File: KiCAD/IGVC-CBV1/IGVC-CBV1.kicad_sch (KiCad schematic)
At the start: 29 parts, among them IC1 STM32F407ZGT6, J1 STLINKV2 PINS (2.54mm Pitch), SW1 SW_SPDT, Y1 EB2532YA12-25.000M_TR

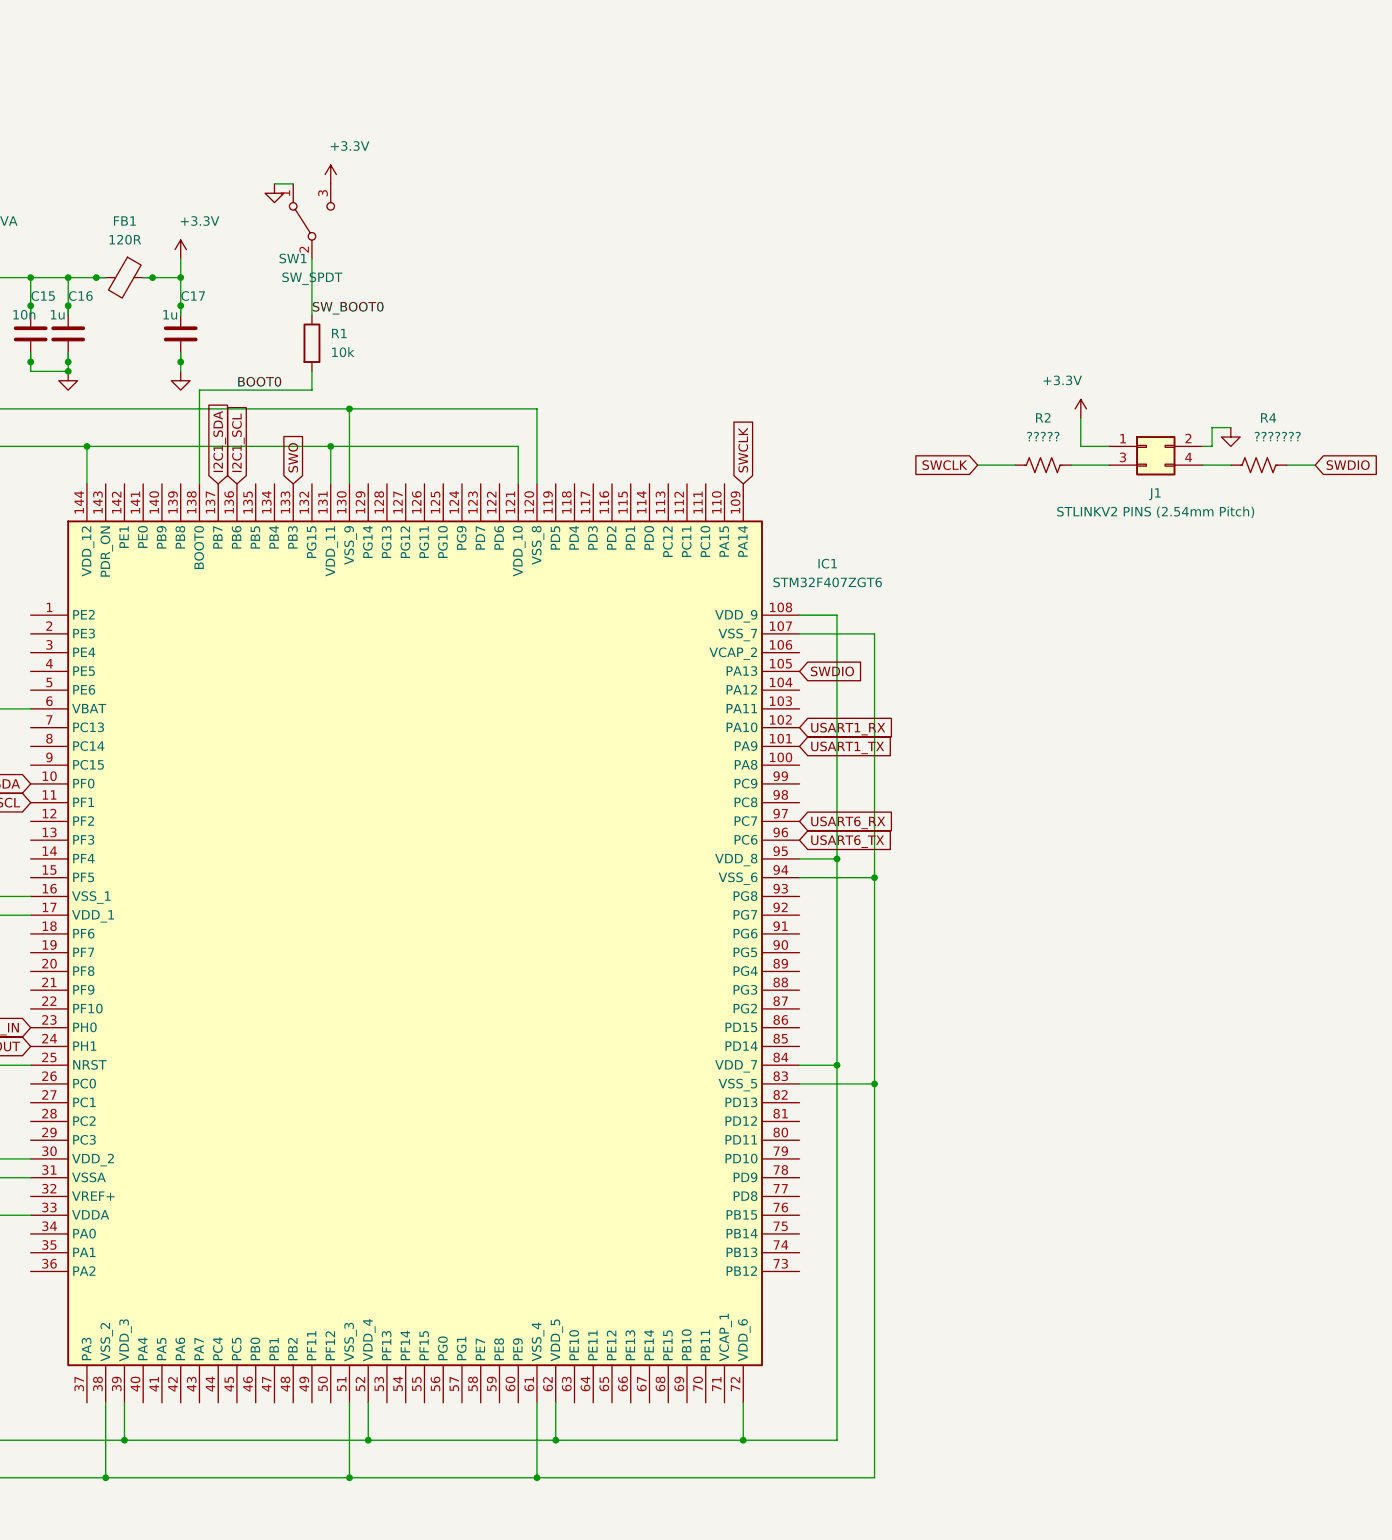
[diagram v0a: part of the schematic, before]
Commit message: 8MB NOR Flash added to schematic with associated docs and files
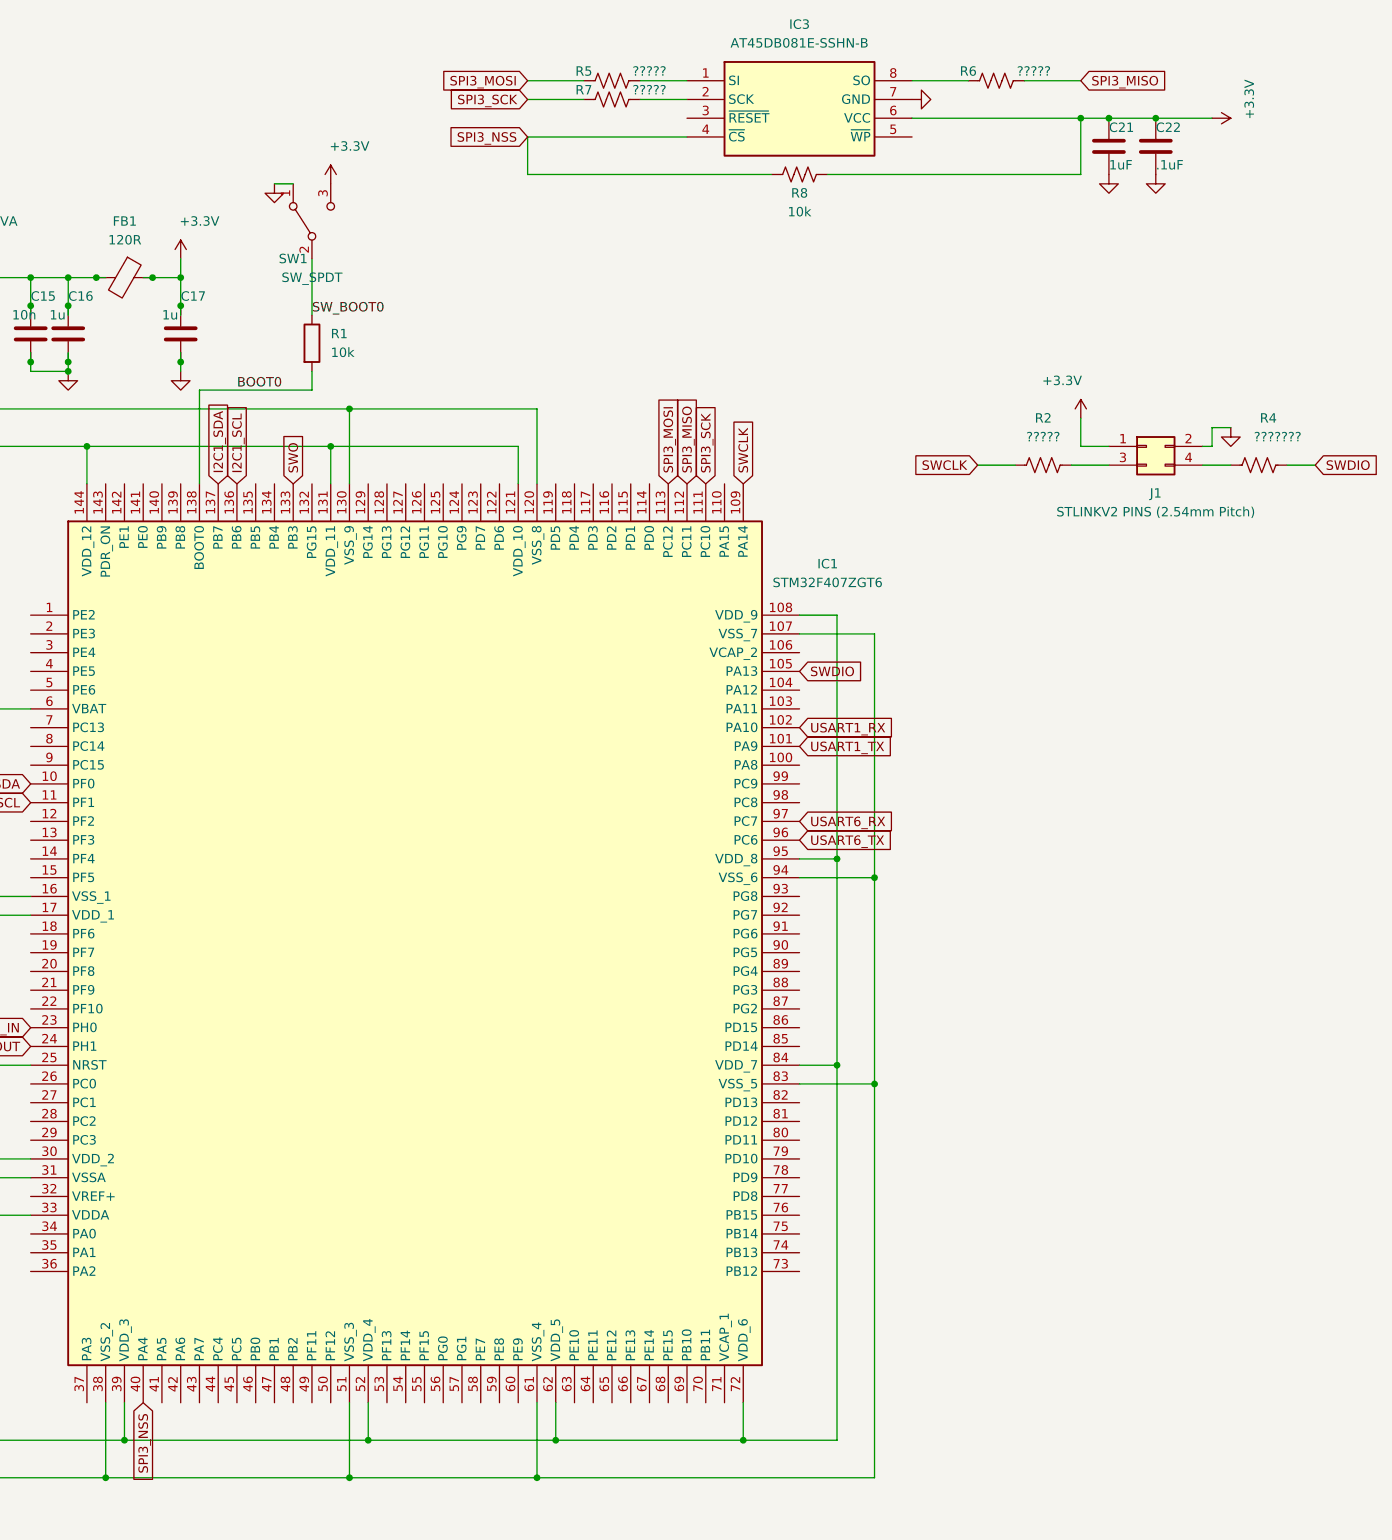
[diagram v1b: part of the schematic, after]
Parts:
- added C21: 1uF, symbol Device:C
- added C22: .1uF, symbol Device:C
- added IC3: AT45DB081E-SSHN-B, SOIC127P600X175-8N, symbol AT45DB081E-SSHN-B:AT45DB081E-SSHN-B
- added R5, R6, R7: ?????, symbol Device:R_US
- added R8: 10k, symbol Device:R_US
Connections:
- net +3.3V: now also C21.1, C22.1, IC3.6 (VCC), R8.2
- net GND: now also C21.2, C22.2, IC3.7 (GND)
- net SPI3_SCK: now reaches IC1.111 (PC10)
- net SPI3_SCK: now also R7.2
- net SPI3_MISO: now reaches IC1.112 (PC11)
- net SPI3_MISO: now also R6.1
- net SPI3_MOSI: now reaches IC1.113 (PC12)
- net SPI3_MOSI: now also R5.2
- net SPI3_NSS: now reaches IC1.40 (PA4)
- net SPI3_NSS: now also IC3.4 (~{CS}), R8.1
- new net: IC3.1 (SI), R5.1
- new net: IC3.2 (SCK), R7.1
- new net: IC3.8 (SO), R6.2

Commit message: Added MD Pins and Cleaned up.
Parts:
- added C13: 1uF, 1 uF:CAPC0603X35N, symbol Device:C
- added C14: 1 uF, 1 uF:CAPC0603X35N, symbol Device:C
- added IC1: SPX3819M5-L-3-3_TR, SOT95P280X145-5N:SOT95P280X145-5N, symbol SPX3819M5-L-3-3_TR:SPX3819M5-L-3-3_TR
- added J1: 12401948E412A, AMPHENOL_12401948E412A:AMPHENOL_12401948E412A, symbol AMPHENOL_12401948E412A:12401948E412A
- added J2: Motor Driver Pins (2.54mm Pitch), symbol Connector_Generic:Conn_02x02_Top_Bottom
- added R11, R14: 5K1, 5k1 Ohms:RESC6432X65N, symbol Device:R_US
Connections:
- net +3.3V: now also C14.1, IC1.5 (VOUT), J2.3 (Pin_3)
- net GND: now also C13.1, C14.2, IC1.2 (GND), J1.A12_B1 (GND), J1.A1_B12 (GND), J1.S1 (SHELL_GND), J1.S2 (SHELL_GND), J1.S3 (SHELL_GND), J1.S4 (SHELL_GND), J2.4 (Pin_4), R11.1, R14.2
- net USART1_RX: now also J2.1 (Pin_1)
- net USART1_TX: now also J2.2 (Pin_2)
- new net: C13.2, IC1.4 (ADJ/BYP)
- new net: J1.A5 (CC1), R11.2
- new net: J1.B5 (CC2), R14.1
- new net VBUS: IC1.1 (VIN), IC1.3 (EN), J1.A4_B9 (VBUS), J1.A9_B4 (VBUS)
- no-connect marks 0 -> 9
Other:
- note added: "8 MB NOR SPI Flash"
- note added: "ALSO, Need a source for Analog Voltage VA. @Colby"
- note added: "Battery Charging & Voltage Regulator (3.3V, 500 mA)"
- note added: "Crystal Oscillator (8 MHz)"
- note added: "LAST Thing: E-Stop. Need to create a way for the EStop to manipulate motor driver w/o MCU processing. This ensures analog intervention as opposed to fluky digital processsing teliing the motors to stop."
- note added: "Motor Driver Pins (2.54mm Pitch)"
- note added: "STLink V2 Pins (2.54mm Pitch)"
- note added: "USB-C (Power Delivery)"
- moved on the sheet: C1, C10, C11, C12, C13, C14, C15, C16, C17, C18, C2, C21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

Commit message: Arduino Pins
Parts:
- added J4: Conn_01x02, symbol Connector_Generic:Conn_01x02
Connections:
- net I2C2_SCL: now also J4.2 (Pin_2)
- net I2C2_SDA: now also J4.1 (Pin_1)
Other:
- note added: "Arduino Connection Pins (2.54mm Pitch)"
- note added: "Voltage Regulator (3.3V, 500 mA)"
- note removed: "Battery Charging & Voltage Regulator (3.3V, 500 mA)"
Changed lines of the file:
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@@
+    (fill (type none))
+  )
+  (rectangle (start 142.24 148.59) (end 190.5 167.64)
+    (stroke (width 0) (type default))
     (fill (type none))
   )
@@
     (effects (font (size 2 2) (thickness 0.254) bold) (justify left bottom))
   )
-  (text "Battery Charging & Voltage Regulator (3.3V, 500 mA)"
-    (at 48.26 114.3 0)
+  (text "Arduino Connection Pins (2.54mm Pitch)" (at 142.24 147.32 0)
+    (effects (font (size 2 2)) (justify left bottom))
+  )
+  (text "Voltage Regulator (3.3V, 500 mA)" (at 48.26 114.3 0)
     (effects (font (size 2 2) (thickness 0.254) bold) (justify left bottom))
   )
@@
     )
   )
+  (global_label "I2C2_SDA" (shape input) (at 166.37 162.56 180) (fields_autoplaced)
+    (effects (font (size 1.27 1.27)) (justify right))
+    (property "Intersheetrefs" "${INTERSHEET_REFS}" (at 154.5553 162.56 0)
+      (effects (font (size 1.27 1.27)) (justify right) hide)
+    )
+  )
   (global_label "RCC_OSC_IN" (shape input) (at 69.85 208.28 180) (fields_autoplaced)
     (effects (font (size 1.27 1.27)) (justify right))
@@
     (effects (font (size 1.27 1.27)) (justify left))
     (property "Intersheetrefs" "${INTERSHEET_REFS}" (at 151.2728 260.35 0)
+      (effects (font (size 1.27 1.27)) (justify left) hide)
+    )
+  )
+  (global_label "I2C2_SCL" (shape input) (at 168.91 162.56 0) (fields_autoplaced)
+    (effects (font (size 1.27 1.27)) (justify left))
+    (property "Intersheetrefs" "${INTERSHEET_REFS}" (at 180.6642 162.56 0)
       (effects (font (size 1.27 1.27)) (justify left) hide)
     )
@@
         )
       )
+    )
+  )
+  (symbol (lib_id "Connector_Generic:Conn_01x02") (at 166.37 157.48 90) (unit 1)
+    (in_bom yes) (on_board yes) (dnp no)
+    (property "Reference" "J4" (at 165.1 151.13 90)
+      (effects (font (size 1.27 1.27)) (justify right))
+    )
+    (property "Value" "Conn_01x02" (at 165.1 153.67 90)
+      (effects (font (size 1.27 1.27)) (justify right))
+    )
+    (property "Footprint" "" (at 166.37 157.48 0)
+      (effects (font (size 1.27 1.27)) hide)
+    )
+    (property "Datasheet" "~" (at 166.37 157.48 0)
+      (effects (font (size 1.27 1.27)) hide)
+    )
+    (pin "1")
+    (pin "2")
+    (instances
+      (project "IGVC-CBV1"
+        (path "/c1e6e0fc-6008-46c6-a177-6e4d31d6ddb3"
+          (reference "J4") (unit 1)
+        )
+      )

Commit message: Draft 5
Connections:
- net +3.3VA is gone; now on net +3.3V: C15.1, C16.1, FB1.2, IC1.33 (VDDA)
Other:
- note added: "Flash Boot"
- note removed: "ALSO, Need a source for Analog Voltage VA. @Colby"
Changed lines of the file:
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@@
     (effects (font (size 2 2) (thickness 0.254) bold) (justify left bottom))
-  )
-  (text "ALSO, Need a source for \nAnalog Voltage VA.\n@Colby"
-    (at 50.8 337.82 0)
-    (effects (font (size 3 3)) (justify left bottom))
   )
   (text "Motor Driver Pins (2.54mm Pitch)" (at 142.24 114.3 0)
@@
   (text "STLink V2 Pins (2.54mm Pitch)" (at 142.24 73.66 0)
     (effects (font (size 2 2) bold) (justify left bottom))
+  )
+  (text "Flash\nBoot" (at 365.76 95.25 0)
+    (effects (font (size 2 2)) (justify left bottom))
   )
   (text "LAST Thing: E-Stop.\nNeed to create a way for the EStop to manipulate\nmotor driver w/o MCU processing.\nThis ensures analog intervention as opposed to\nfluky digital processsing teliing the motors\nto stop."
@@
         (path "/c1e6e0fc-6008-46c6-a177-6e4d31d6ddb3"
           (reference "C1") (unit 1)
-        )
-      )
-    )
-  )
-  (symbol (lib_id "power:+3.3VA") (at 331.47 106.68 0) (unit 1)
-    (in_bom yes) (on_board yes) (dnp no) (fields_autoplaced)
-    (property "Reference" "#PWR05" (at 331.47 110.49 0)
-      (effects (font (size 1.27 1.27)) hide)
-    )
-    (property "Value" "+3.3VA" (at 331.47 101.6 0)
-      (effects (font (size 1.27 1.27)))
-    )
-    (property "Footprint" "" (at 331.47 106.68 0)
-      (effects (font (size 1.27 1.27)) hide)
-    )
-    (property "Datasheet" "" (at 331.47 106.68 0)
-      (effects (font (size 1.27 1.27)) hide)
-    )
-    (pin "1")
-    (instances
-      (project "IGVC_PCB"
-        (path "/ba927162-b9f6-45a7-80b2-ebd881f388a6"
-          (reference "#PWR05") (unit 1)
-        )
-      )
-      (project "IGVC-CBV1"
-        (path "/c1e6e0fc-6008-46c6-a177-6e4d31d6ddb3"
-          (reference "#PWR05") (unit 1)
         )
       )
@@
   (symbol (lib_id "Switch:SW_SPDT") (at 374.65 101.6 90) (unit 1)
     (in_bom yes) (on_board yes) (dnp no)
-    (property "Reference" "SW1" (at 372.11 106.68 90)
-      (effects (font (size 1.27 1.27)))
-    )
-    (property "Value" "SW_SPDT" (at 374.65 109.22 90)
+    (property "Reference" "SW1" (at 384.81 99.06 90)
+      (effects (font (size 1.27 1.27)))
+    )
+    (property "Value" "SW_SPDT" (at 387.35 101.6 90)
       (effects (font (size 1.27 1.27)))
     )
@@
         )
       )
+    )
+  )
+  (symbol (lib_id "power:+3.3V") (at 331.47 106.68 0) (unit 1)
+    (in_bom yes) (on_board yes) (dnp no)
+    (property "Reference" "#PWR02" (at 331.47 110.49 0)
+      (effects (font (size 1.27 1.27)) hide)
+    )
+    (property "Value" "+3.3V" (at 332.74 101.6 0)
+      (effects (font (size 1.27 1.27)))
+    )
+    (property "Footprint" "" (at 331.47 106.68 0)
+      (effects (font (size 1.27 1.27)) hide)
+    )
+    (property "Datasheet" "" (at 331.47 106.68 0)
+      (effects (font (size 1.27 1.27)) hide)
+    )
+    (pin "1")
+    (instances
+      (project "IGVC_PCB"
+        (path "/ba927162-b9f6-45a7-80b2-ebd881f388a6"
+          (reference "#PWR02") (unit 1)
+        )
+      )
+      (project "IGVC-CBV1"
+        (path "/c1e6e0fc-6008-46c6-a177-6e4d31d6ddb3"
+          (reference "#PWR05") (unit 1)
+        )
+      )

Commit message: yup
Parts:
- R5, R6, R7: value ????? -> 0 Ohm
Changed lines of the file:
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@@
       (effects (font (size 1.27 1.27)))
     )
-    (property "Value" "?????" (at 132.08 259.08 90)
+    (property "Value" "0 Ohm" (at 132.08 259.08 90)
       (effects (font (size 1.27 1.27)))
     )
@@
       (effects (font (size 1.27 1.27)))
     )
-    (property "Value" "?????" (at 80.01 259.08 90)
+    (property "Value" "0 Ohm" (at 80.01 259.08 90)
       (effects (font (size 1.27 1.27)))
     )
@@
       (effects (font (size 1.27 1.27)))
     )
-    (property "Value" "?????" (at 80.01 261.62 90)
-      (effects (font (size 1.27 1.27)))
-    )
+    (property "Value" "0 Ohm" (at 80.01 261.62 90)
+      (effects (font (size 1.27 1.27)))
+    )

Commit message: Schematic DONE!! PCB BEGINS!
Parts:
- removed R2: ?????, symbol Device:R_US
- removed R4: ???????, symbol Device:R_US
- C1, C10, C11, C12, C13, C18, C2, C22, C3, C4, C5, C6, C7, C8, C9: footprint (none) -> LIB_08051C104K4Z2A:CAPC2012X140N
- C13, C14: footprint 1 uF:CAPC0603X35N -> LIB_GRMMDXR60J105ME05D:CAPC0502X28N
- C14: footprint (none) -> LIB_C0402C120F5GAC7867:CAPC1005X55N
- C14: footprint (none) -> LIB_T491A106K010AT:T491A
- C15: footprint (none) -> C0603C103K4RECTU:CAPC17595_87N_KEM
- C16, C17, C21: footprint (none) -> LIB_GRMMDXR60J105ME05D:CAPC0502X28N
- FB1: footprint (none) -> LIB_BLM15PX121BH1D:NFZ15SG152SN10B
- IC1: footprint SOT95P280X145-5N:SOT95P280X145-5N -> LIB_SPX3819M5-L-3-3_TR:SOT95P280X145-5N
- IC1: footprint QFP50P2200X2200X160-144N -> LIB_STM32F407ZGT6:QFP50P2200X2200X160-144N
- IC3: footprint SOIC127P600X175-8N -> LIB_AT45DB081E-SSHN-B:SOIC127P600X175-8N
- J1, J2: footprint (none) -> LIB_47053-1000:470531000
- J1: footprint AMPHENOL_12401948E412A:AMPHENOL_12401948E412A -> 12401948E412A:AMPHENOL_12401948E412A
- J4: footprint (none) -> LIB_22-12-2024:22122024
- R1, R8: footprint (none) -> RC0402FR-0710KL:RESC1005X40N
- R11, R14: footprint 5k1 Ohms:RESC6432X65N -> LIB_ERA-3VEB5101V:ERA3KV__0603_
- R3: footprint (none) -> LIB_CRCW120660R0KNEAIF:RESC3216X60N
- R5, R6, R7: footprint (none) -> LIB_ERJ-1GJ0R00C:ERJ1G_1023
- SW1: footprint (none) -> 1101M2S3CQE2:1101M2S3CQE2
- Y1: footprint EB2532YA1225000MTR -> LIB_EB2532YA12-25.000M_TR:EB2532YA1225000MTR
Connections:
- net SWCLK: now also J1.3 (Pin_3)
- net SWDIO: now also J1.4 (Pin_4)
- net I2C1_SCL: no longer names the net of IC1.136 (PB6)
- net I2C1_SDA: no longer names the net of IC1.137 (PB7)
- net SWO: no longer names the net of IC1.133 (PB3)
- net USART6_RX: no longer names the net of IC1.97 (PC7)
- net USART6_TX: no longer names the net of IC1.96 (PC6)
- no-connect marks 9 -> 115
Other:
- note added: "Crystal Oscillator (25 MHz)"
- note removed: "Crystal Oscillator (8 MHz)"
- company: (none) -> Evan Eden, Colby McLane, Kerwin Zhang, Tarun Daggolu
- title: (none) -> Arduino Replacement V1
